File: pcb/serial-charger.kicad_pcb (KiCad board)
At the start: 2 copper layers, 87 x 21 mm, 69 parts, among them IC201 ATMEGA328P-M, IC401 CH340G, J101 jumper, J102 jumper, P101 USB_OTG, P102 CONN_01X02, P103 CONN_01X04, P201 CONNECTOR, P202 CONNECTOR, P203 CONNECTOR, P204 CONNECTOR, P205 CONNECTOR, P206 CONNECTOR, P207 CONNECTOR, P208 CONNECTOR, P209 CONNECTOR, P210 CONNECTOR, P211 CONNECTOR, P212 CONNECTOR, P213 CONNECTOR, P214 CONNECTOR, P215 CONNECTOR, P216 CONNECTOR, P217 CONNECTOR, P218 CONNECTOR, P219 CONNECTOR, P220 CONNECTOR, P221 CONNECTOR, P222 CONN_01X03, P223 CONNECTOR, P224 CONNECTOR, SW201 SW_PUSH, U101 XC6206, U301 FM6316FE, x201 xtal_osc, x401 xtal_osc

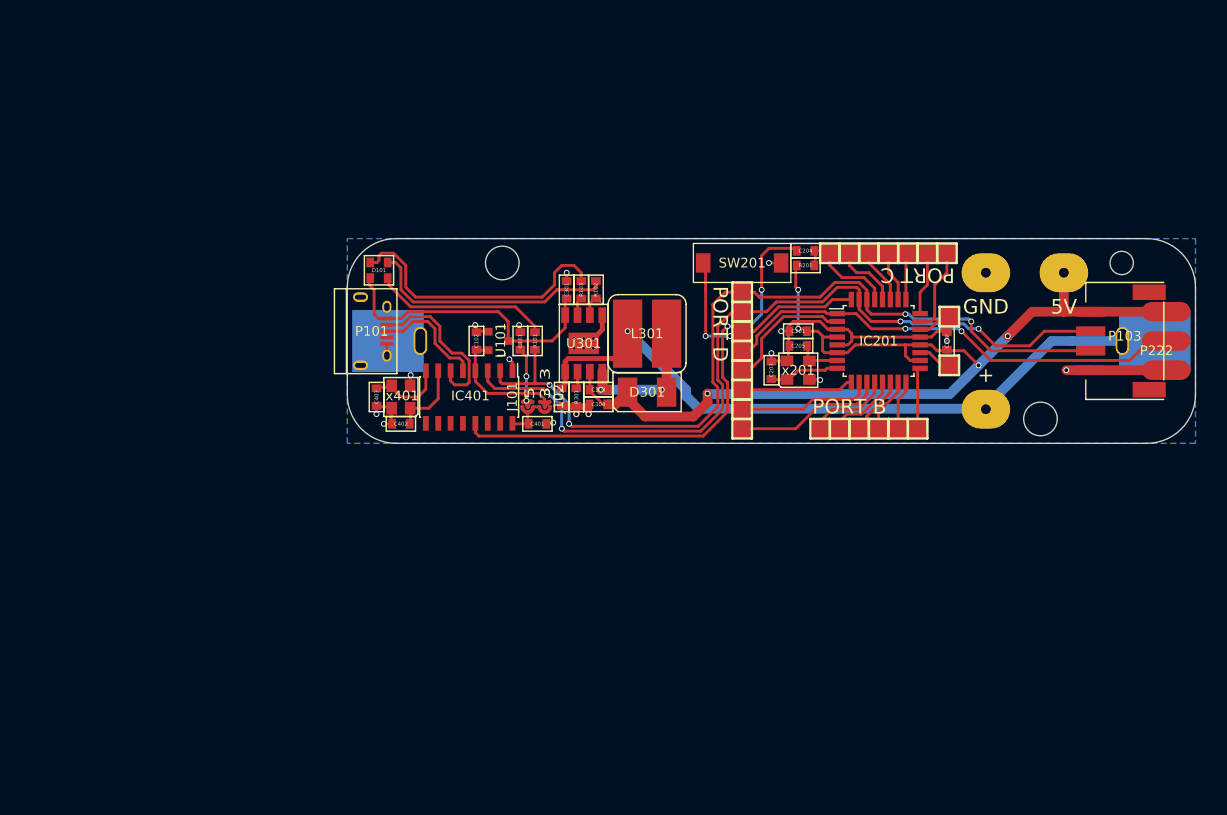
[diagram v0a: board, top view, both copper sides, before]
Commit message: reworked bms and mcu to use seeed components
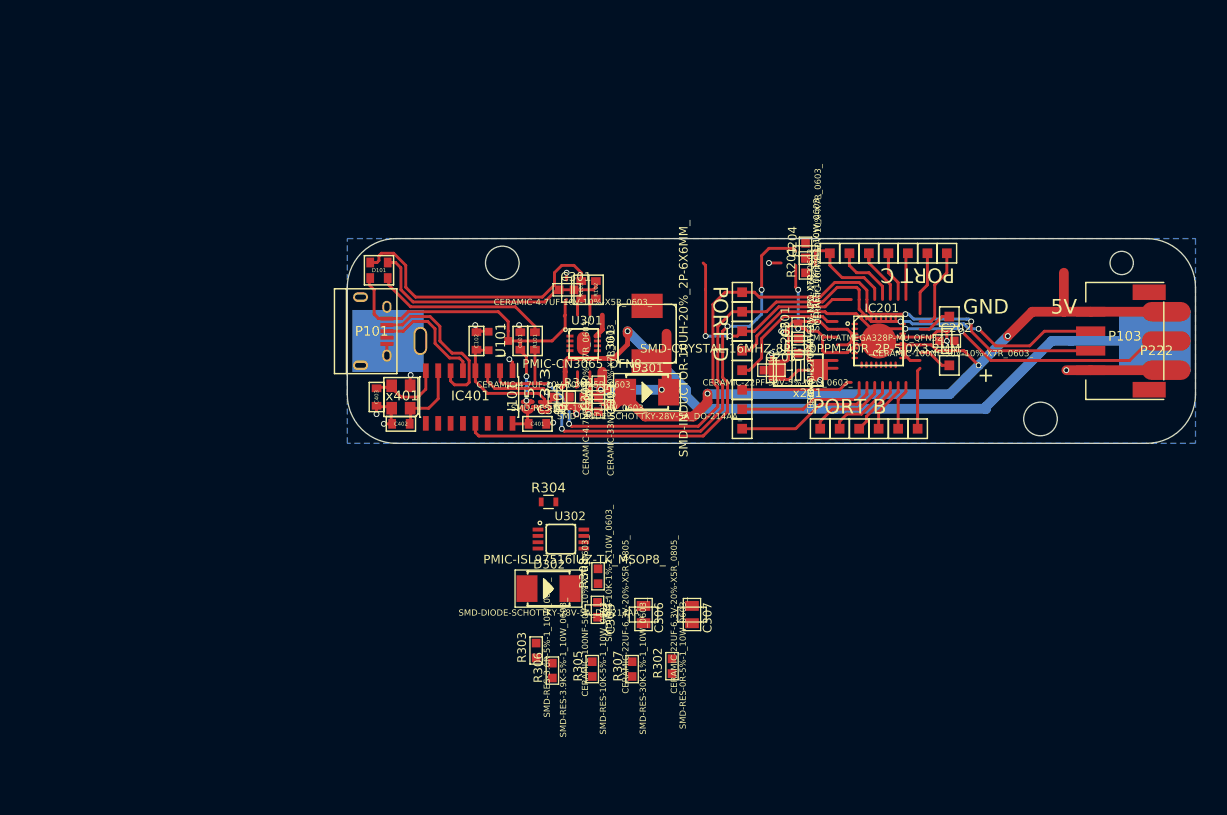
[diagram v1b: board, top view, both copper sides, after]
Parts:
- removed the REF** at (172.0, 107.0)
- removed the REF** at (180.0, 93.0)
- removed the REF** at (172.0, 93.0)
- removed the REF** at (186.0, 100.0)
- removed the REF** at (129.8, 99.8)
- removed the REF** at (130.8, 99.8)
- removed the REF** at (131.8, 99.8)
- removed the REF** at (131.8, 100.8)
- removed the REF** at (130.8, 100.8)
- removed the REF** at (129.8, 100.8)
- removed SW201: SW_PUSH, netl:Button
- added C305: CERAMIC-100NF-50V-10%-X7R_0603_, SeeedOPL-Capacitor-2016:C0603, F.Cu at (132.2, 127.6)
- added C306: CERAMIC-22UF-6.3V-20%-X5R_0805_, SeeedOPL-Capacitor-2016:C0805, F.Cu at (136.9, 128.1)
- added C307: CERAMIC-22UF-6.3V-20%-X5R_0805_, SeeedOPL-Capacitor-2016:C0805, F.Cu at (141.9, 128.1)
- added D302: SMD-DIODE-SCHOTTKY-28V-5A_DO-214AA_, SeeedOPL-Diode-2016:DO-214AA, F.Cu at (127.1, 125.4)
- added R302: SMD-RES-0R-5%-1_10W_0603_, SeeedOPL-Resistor-2016:R0603, F.Cu at (139.8, 133.4)
- added R303: SMD-RES-3.6R-5%-1_10W_0603_, SeeedOPL-Resistor-2016:R0603, F.Cu at (125.9, 131.8)
- added R304: SMD-RES-0R-5%-1_10W_0603_, Resistors_SMD:R_0603, F.Cu at (127.1, 116.5)
- added R305: SMD-RES-10K-5%-1_10W_0603_, SeeedOPL-Resistor-2016:R0603, F.Cu at (131.6, 133.7)
- added R306: SMD-RES-3.9K-5%-1_10W_0603_, SeeedOPL-Resistor-2016:R0603, F.Cu at (127.5, 133.8)
- added R307: SMD-RES-30K-1%-1_10W_0603_, SeeedOPL-Resistor-2016:R0603, F.Cu at (135.7, 133.7)
- added R308: SMD-RES-10K-1%-1_10W_0603_, SeeedOPL-Resistor-2016:R0603, F.Cu at (132.2, 124.1)
- added U302: PMIC-ISL97516IUZ-TK_MSOP8_, SeeedOPL-IC-2016:MSOP8-0.65-3X3MM, F.Cu at (128.4, 120.3)
- C201, C202, C204: value 100n -> CERAMIC-100NF-50V-10%-X7R_0603_; footprint netl:SMD_0603 -> SeeedOPL-Capacitor-2016:C0603
- C203, C205: value 22p -> CERAMIC-22PF-50V-5%-NPO_0603_; footprint netl:SMD_0603 -> SeeedOPL-Capacitor-2016:C0603
- C301, C302: value 10u -> CERAMIC-4.7UF-10V-10%-X5R_0603_; footprint netl:SMD_0603 -> SeeedOPL-Capacitor-2016:C0603
- C303: value 2n -> CERAMIC-4.7NF-50V-10%-X7R_0603_; footprint netl:SMD_0603 -> SeeedOPL-Capacitor-2016:C0603
- C304: value 47u -> CERAMIC-33NF-50V-10%-X7R_0603_; footprint netl:SMD_0603 -> SeeedOPL-Capacitor-2016:C0603
- D301: value 1N5822 -> SMD-DIODE-SCHOTTKY-28V-5A_DO-214AA_; footprint netl:DO-214AC -> SeeedOPL-Diode-2016:DO-214AA
- IC201: value ATMEGA328P-M -> MCU-ATMEGA328P-MU_QFN32_; footprint Housings_QFP:TQFP-32_7x7mm_Pitch0.8mm -> SeeedOPL-IC-2016:QFN32G-0.5-5X5MM
- L301: value 3.3u -> SMD-INDUCTOR-10UH-20%_2P-6X6MM_; footprint netl:7x7_Inductor -> SeeedOPL-Inductor-2016:SMD-2P-L6.0XW6.0XH3.0MM
- P201, P202, P203, P204, P205, P206, P207, P208, P209, P210, P211, P212, P213, P214, P215, P216, P217, P218, P219, P220, P221, P223, P224: footprint netl:1Pin_big -> netl:1Pin_small
- R201: value 10k -> SMD-RES-10K-1%-1_10W_0603_; footprint netl:SMD_0603 -> SeeedOPL-Resistor-2016:R0603
- R301: value 2k -> SMD-RES-10K-1%-1_10W_0603_; footprint netl:SMD_0603 -> SeeedOPL-Resistor-2016:R0603
- U301: value FM6316FE -> PMIC-CN3065_DFN8_; footprint netl:ESOP-8 -> SeeedOPL-IC-2016:DFN8G-0.5-3X3MM
- x201: value xtal_osc -> SMD-CRYSTAL-16MHZ-8PF-20PPM-40R_2P-5.0X3.2MM_; footprint netl:SM_3225 -> SeeedOPL-Crystal Oscillator-2016:X2-SMD-5.0X3.2X1.3MM
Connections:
- net /USB to Serial/3V3 renamed /3V3
- net /USB to Serial/D+ renamed /D+
- net /USB to Serial/D- renamed /D-
- net /USB to Serial/RX renamed /RX
- net /USB to Serial/V_SER renamed /V_SER
- net /avr/RX renamed /TX
- C101 pad 1: /Battery Management/5V_IN -> /V_USB
- C201 pad 1: /Battery Management/5V_OUT -> /avr/VCC
- C202 pad 1: /Battery Management/5V_OUT -> /avr/VCC
- C203 pad 1: /avr/XTAL1 -> GND
- C203 pad 2: GND -> /avr/XTAL1
- C204 pad 1: /avr/~RESET -> /~DTR
- C204 pad 2: /USB to Serial/~DTR -> /avr/~RESET
- C205 pad 1: /avr/XTAL2 -> GND
- C205 pad 2: GND -> /avr/XTAL2
- C301 pad 1: /Battery Management/5V_IN -> GND
- C301 pad 2: GND -> /V_USB
- C302 pad 1: /Battery Management/V_BAT -> GND
- C302 pad 2: GND -> /V_BAT
- C303 pad 1: /Battery Management/5V_OUT -> (no net)
- C303 pad 2: Net-(C303-Pad2) -> (no net)
- C304 pad 1: /Battery Management/5V_OUT -> GND
- C304 pad 2: GND -> Net-(C304-Pad2)
- D101 pad 4: /Battery Management/5V_IN -> /V_USB
- IC201 pad 18: /Battery Management/5V_OUT -> /avr/VCC
- IC201 pad 20: /Battery Management/5V_OUT -> /avr/VCC
- IC201 pad 4: /Battery Management/5V_OUT -> /avr/VCC
- IC201 pad 6: /Battery Management/5V_OUT -> /avr/VCC
- IC201 pad 7: /avr/XTAL2 -> /avr/XTAL1
- IC201 pad 8: /avr/XTAL1 -> /avr/XTAL2
- IC401 pad 13: /USB to Serial/~DTR -> /~DTR
- J101 pad 1: /Battery Management/5V_IN -> /V_USB
- L301 pad 1: /Battery Management/V_BAT -> /V_BAT
- L301 pad 2: Net-(C303-Pad2) -> Net-(D302-Pad+)
- P101 pad 1: /Battery Management/5V_IN -> /V_USB
- P102 pad 2: /Battery Management/V_BAT -> /V_BAT
- P103 pad 4: /Battery Management/5V_OUT -> /5V
- P222 pad 1: /Battery Management/5V_OUT -> /avr/VCC
- R102 pad 1: /Battery Management/~stby -> /~stby
- R103 pad 1: /Battery Management/~chrg -> /~chrg
- R201 pad 1: /Battery Management/5V_OUT -> /avr/VCC
- R301 pad 2: GND -> /V_USB
- U101 pad 3: /Battery Management/5V_IN -> /V_USB
- U301 pad 1: GND -> Net-(R301-Pad1)
- U301 pad 2: /Battery Management/~stby -> Net-(R303-Pad2)
- U301 pad 3: /Battery Management/~chrg -> GND
- U301 pad 4: /Battery Management/5V_IN -> /V_USB
- U301 pad 5: /Battery Management/V_BAT -> /V_BAT
- U301 pad 6: Net-(R301-Pad1) -> /~stby
- U301 pad 7: /Battery Management/5V_OUT -> /~chrg
- U301 pad 8: Net-(C303-Pad2) -> Net-(R304-Pad1)
- x201 pad 2: GND -> /avr/XTAL2
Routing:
- net /V_USB: track 0.00 -> 112.9 mm, vias 0 -> 5
- net /Battery Management/5V_OUT: track 106.3 -> 0.00 mm, vias 5 -> 0
- net /V_BAT: track 0.00 -> 76.6 mm, vias 0 -> 1
- net /Battery Management/V_BAT: track 76.6 -> 0.00 mm, vias 1 -> 0
- net /~DTR: track 0.00 -> 51.1 mm, vias 0 -> 2
- net /USB to Serial/~DTR: track 51.1 -> 0.00 mm, vias 2 -> 0
- net /Battery Management/5V_IN: track 38.5 -> 0.00 mm, vias 2 -> 0
- net /5V: track 0.00 -> 28.1 mm, vias 0 -> 2
- net Net-(IC201-Pad33): track 0.00 -> 27.1 mm, vias 0 -> 2
- net Net-(D101-Pad2): track 25.6 -> 1.45 mm
- net Net-(C303-Pad2): track 17.6 -> 0.00 mm, vias 2 -> 0
- net (no net): track 0.00 -> 12.7 mm, vias 0 -> 4
- net GND: track 64.6 -> 74.6 mm, vias 16 -> 10
- net /avr/LED_SRIP: track 49.5 -> 43.8 mm, vias 2 -> 1
- net Net-(R304-Pad1): track 0.00 -> 2.42 mm
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
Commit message: finished swapping parts, started layout
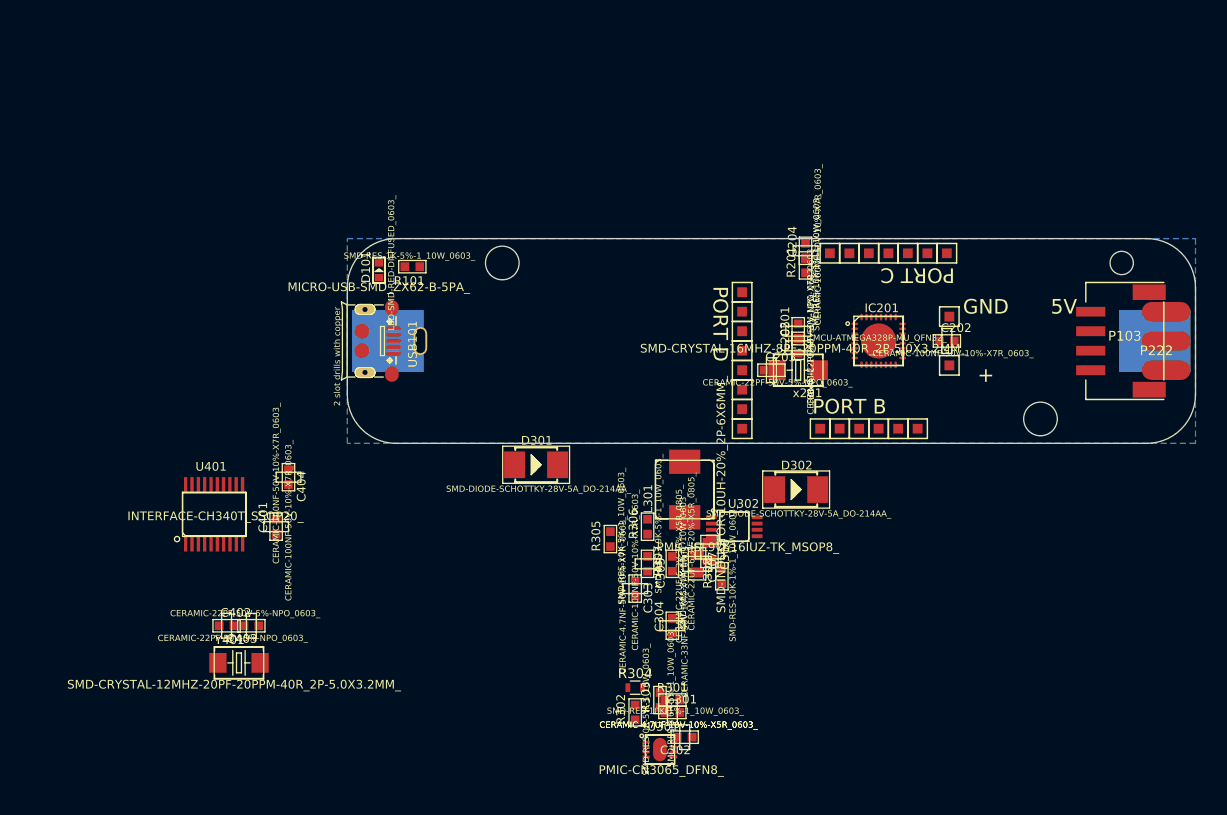
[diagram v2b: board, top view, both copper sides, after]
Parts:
- removed C101, C102: 10u, netl:SMD_0603
- removed IC401: CH340G, Housings_SOIC:SOIC-16_3.9x9.9mm_Pitch1.27mm
- removed J101, J102: jumper, netl:Jumper
- removed P101: USB_OTG, Connect:USB_Micro-B
- removed R102, R103: 1k, netl:SMD_0603
- removed U101: XC6206, TO_SOT_Packages_SMD:SOT-23
- removed x401: xtal_osc, netl:SM_3225
- added C404: CERAMIC-100NF-50V-10%-X7R_0603_, SeeedOPL-Capacitor-2016:C0603, F.Cu at (100.5, 114.0)
- added U401: INTERFACE-CH340T_SSOP20_, SeeedOPL-IC-2016:TSSOP20-0.65-6.5X4.4MM, F.Cu at (92.8, 117.8)
- added USB101: MICRO-USB-SMD_ZX62-B-5PA_, SeeedOPL-Connector-2016:MICRO-USB5+4P-SMD-0.65-B, F.Cu at (111.5, 100.0)
- added Y401: SMD-CRYSTAL-12MHZ-20PF-20PPM-40R_2P-5.0X3.2MM_, SeeedOPL-Crystal Oscillator-2016:X2-SMD-5.0X3.2X1.3MM, F.Cu at (95.4, 133.0)
- C401: value 10u -> CERAMIC-100NF-50V-10%-X7R_0603_; footprint netl:SMD_0603 -> SeeedOPL-Capacitor-2016:C0603
- C402, C403: value 22p -> CERAMIC-22PF-50V-5%-NPO_0603_; footprint netl:SMD_0603 -> SeeedOPL-Capacitor-2016:C0603
- D101: value RGB_LED -> LED-SMD-RED-DIFFUSED_0603_; footprint netl:SMD_0606 -> SeeedOPL-LED-2016:LED-0603
- R101: value 1k -> SMD-RES-1K-5%-1_10W_0603_; footprint netl:SMD_0603 -> SeeedOPL-Resistor-2016:R0603
- moved C301 44.7 mm to (139.8, 138.1)
- moved U301 42.4 mm to (138.6, 141.9)
- moved C302 37.1 mm to (141.1, 140.6)
- moved R301 32.6 mm to (139.8, 136.8)
- moved C401 28.8 mm to (99.2, 119.0)
- moved C402 27.4 mm to (94.1, 129.2), turned to 90 degrees
- moved D302 27.4 mm to (152.5, 115.2)
- moved C403 26.7 mm to (96.7, 129.2)
- moved C304 23.9 mm to (139.8, 129.2)
- moved R304 21.0 mm to (136.0, 135.6)
- moved C303 20.7 mm to (136.0, 125.4)
- moved U302 17.8 mm to (146.2, 119.0)
- moved R306 17.7 mm to (137.3, 119.0)
- moved L301 16.4 mm to (141.1, 115.2)
- moved R101 14.7 mm to (113.2, 92.4)
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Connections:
- net Net-(IC201-Pad15) renamed /avr/MOSI
- net Net-(IC201-Pad16) renamed /avr/MISO
- net Net-(IC201-Pad17) renamed /avr/SCK
- C201 pad 1: /avr/VCC -> /5V
- C202 pad 1: /avr/VCC -> /5V
- C401 pad 2: /V_SER -> /3V3
- C402 pad 1: Net-(C402-Pad1) -> GND
- C402 pad 2: GND -> Net-(C402-Pad2)
- C403 pad 1: Net-(C403-Pad1) -> GND
- C403 pad 2: GND -> Net-(C403-Pad2)
- IC201 pad 18: /avr/VCC -> /5V
- IC201 pad 20: /avr/VCC -> /5V
- IC201 pad 33: Net-(IC201-Pad33) -> GND
- IC201 pad 4: /avr/VCC -> /5V
- IC201 pad 6: /avr/VCC -> /5V
- P222 pad 1: /avr/VCC -> /5V
- R101 pad 1: /TX -> Net-(D101-Pad-)
- R101 pad 2: Net-(D101-Pad3) -> /~chrg
- R201 pad 1: /avr/VCC -> /5V
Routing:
- net /V_USB: track 112.9 -> 0.00 mm, vias 5 -> 0
- net /TX: track 86.4 -> 0.00 mm, vias 4 -> 0
- net /RX: track 82.7 -> 0.00 mm, vias 4 -> 0
- net /V_BAT: track 76.6 -> 0.00 mm, vias 1 -> 0
- net GND: track 74.6 -> 0.00 mm, vias 10 -> 0
- net /~DTR: track 51.1 -> 0.00 mm, vias 2 -> 0
- net /avr/LED_SRIP: track 43.8 -> 0.00 mm, vias 1 -> 0
- net Net-(D101-Pad1): track 28.8 -> 0.00 mm
- net /5V: track 28.1 -> 0.00 mm, vias 2 -> 0
- net Net-(IC201-Pad33): track 27.1 -> 0.00 mm, vias 2 -> 0
- net /avr/BTN: track 24.1 -> 0.00 mm, vias 2 -> 0
- net Net-(D101-Pad3): track 18.0 -> 0.00 mm
- net /D-: track 17.0 -> 0.00 mm
- net Net-(IC201-Pad11): track 15.5 -> 0.00 mm
- net /3V3: track 15.0 -> 0.00 mm
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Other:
- board text removed: "5 3.3"
- board text removed: "Greets: hacklab.fi, nakkiservo, Elite Dekkerz"

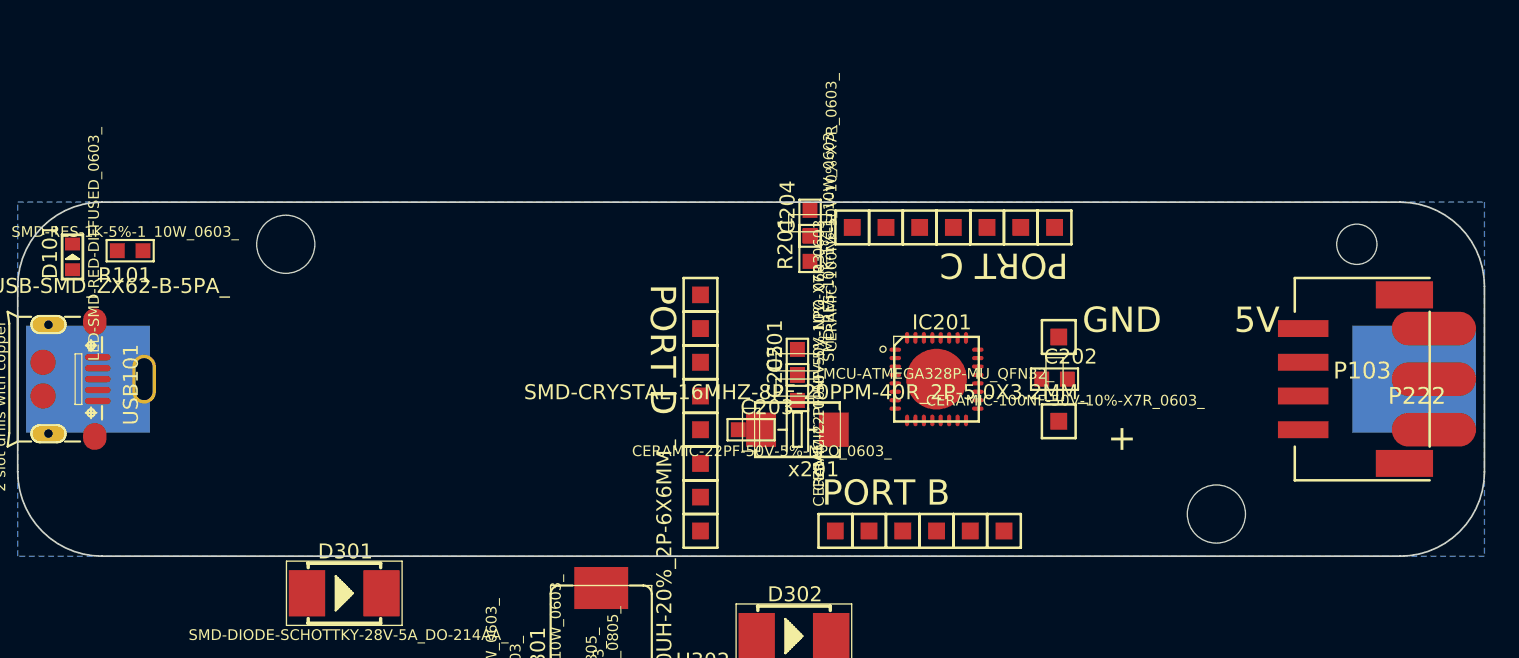
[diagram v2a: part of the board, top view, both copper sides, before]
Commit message: added led strip power control, minor adjustments to layout
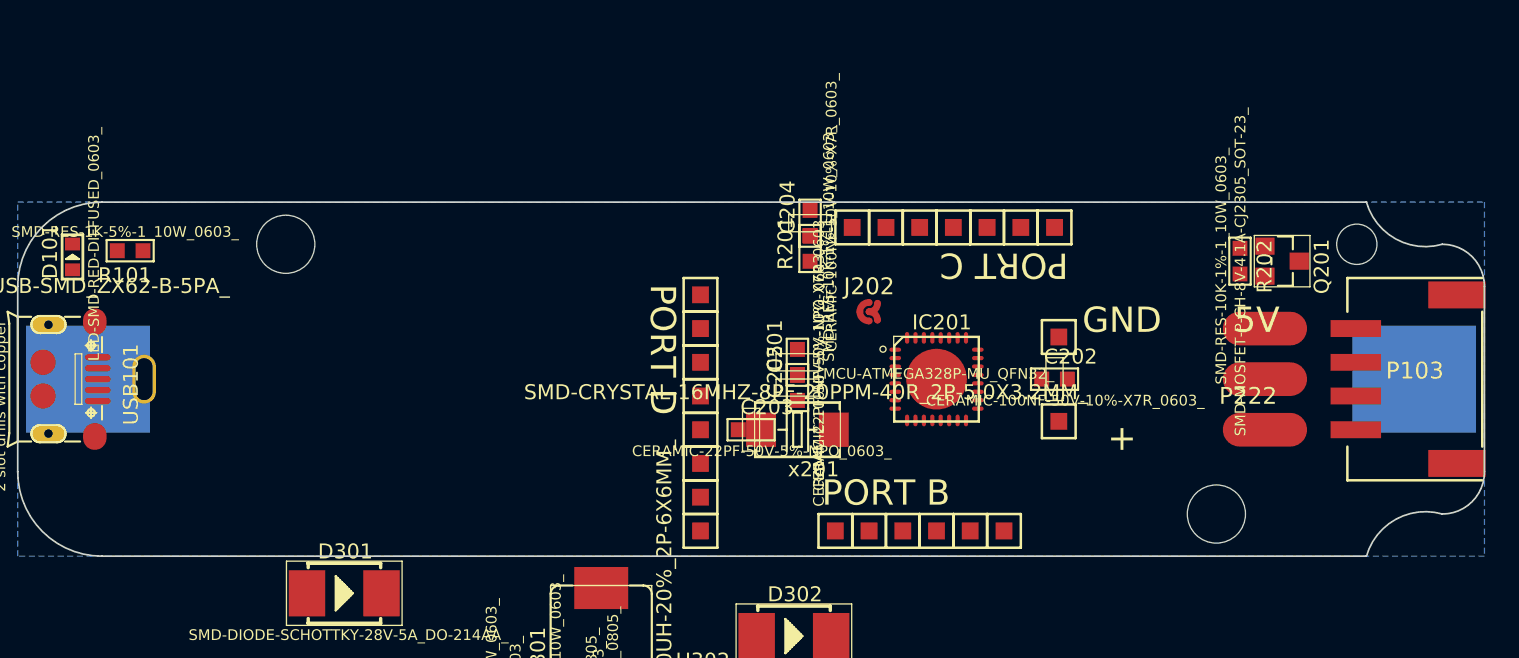
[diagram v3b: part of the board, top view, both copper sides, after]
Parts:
- added J202: jumper, netl:Jumper, F.Cu at (157.0, 96.0)
- added Q201: SMD-MOSFET-P-CH-8V-4.1A-CJ2305_SOT-23_, SeeedOPL-Transistor-2016:SOT-23, F.Cu at (181.5, 93.0)
- added R202: SMD-RES-10K-1%-1_10W_0603_, SeeedOPL-Resistor-2016:R0603, F.Cu at (179.0, 93.0)
- moved P222 10.0 mm to (180.5, 100.0)
- moved P103 3.12 mm to (189.4, 100.0)
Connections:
- net /avr/LED_SRIP renamed /avr/LED_DATA
- net Net-(IC201-Pad2) renamed /avr/~LED_ENABLE
- P222 pad 1: /5V -> Net-(P222-Pad1)
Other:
- outline, holes or cut-outs redrawn
